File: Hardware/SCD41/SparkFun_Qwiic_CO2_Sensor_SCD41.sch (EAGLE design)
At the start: 26 parts, among them J1 QWIIC_RA, J2 QWIIC_RA, J3 PTH, U1 SCD40/1, U6 SCD40, U7 SCD41

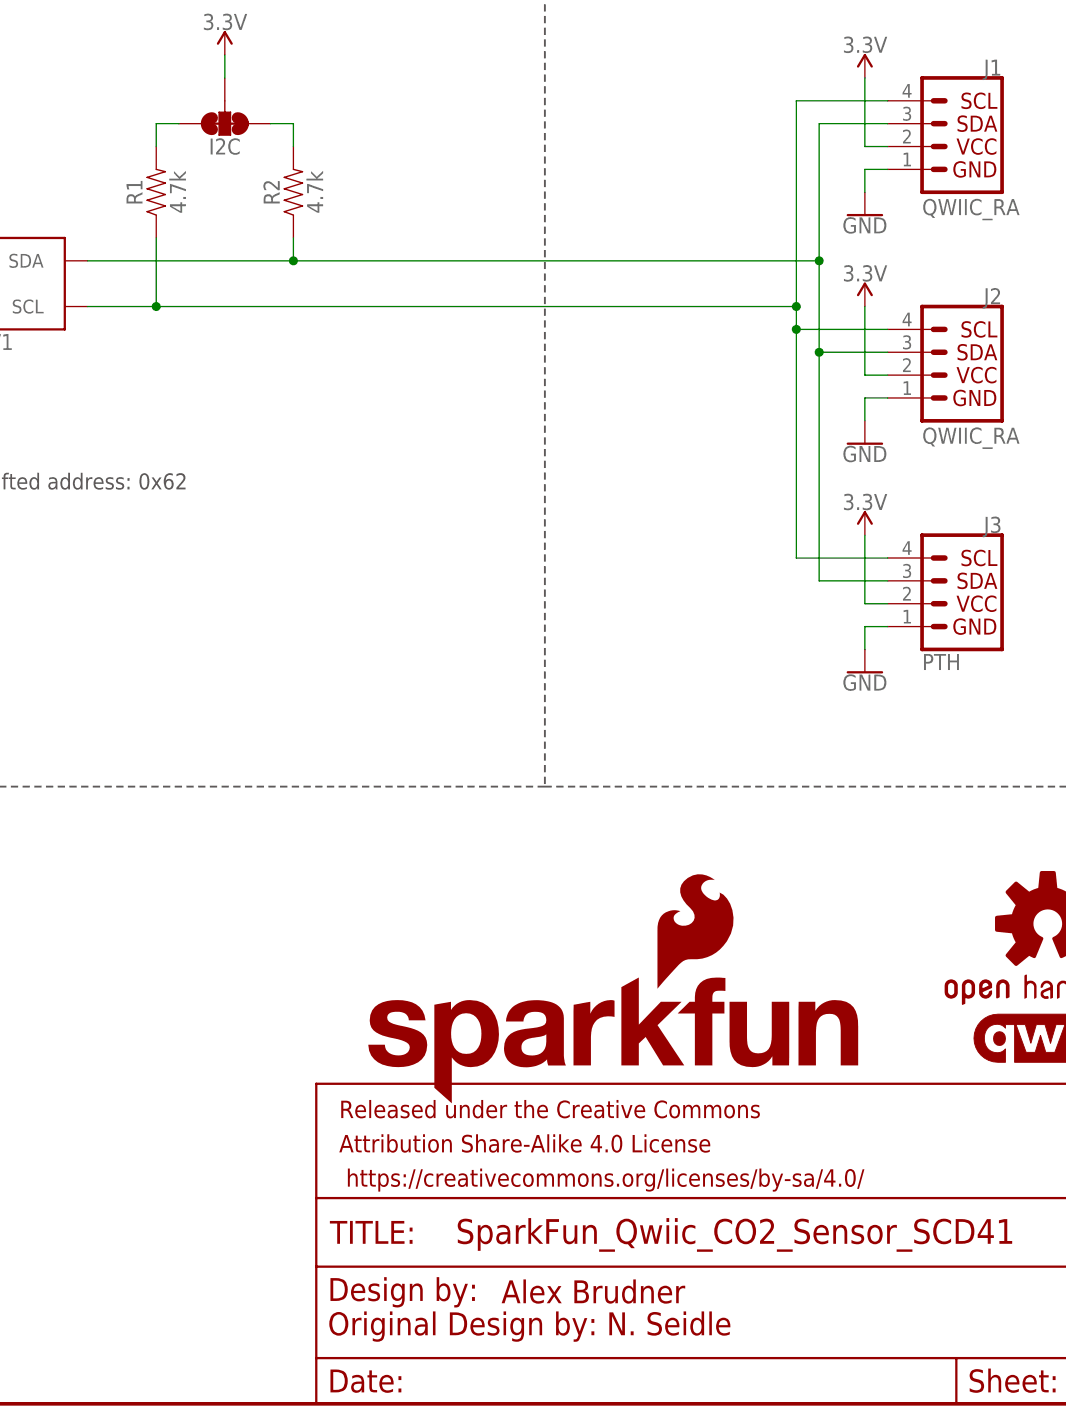
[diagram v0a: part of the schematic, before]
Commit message: Update from pre-design review notes.
Changed I2C PURs from 4.7k to 2.2k to match Qwiic standards.
Changed wording on revision.
Update top stop of pin 1 of sensor.
Repanelize.
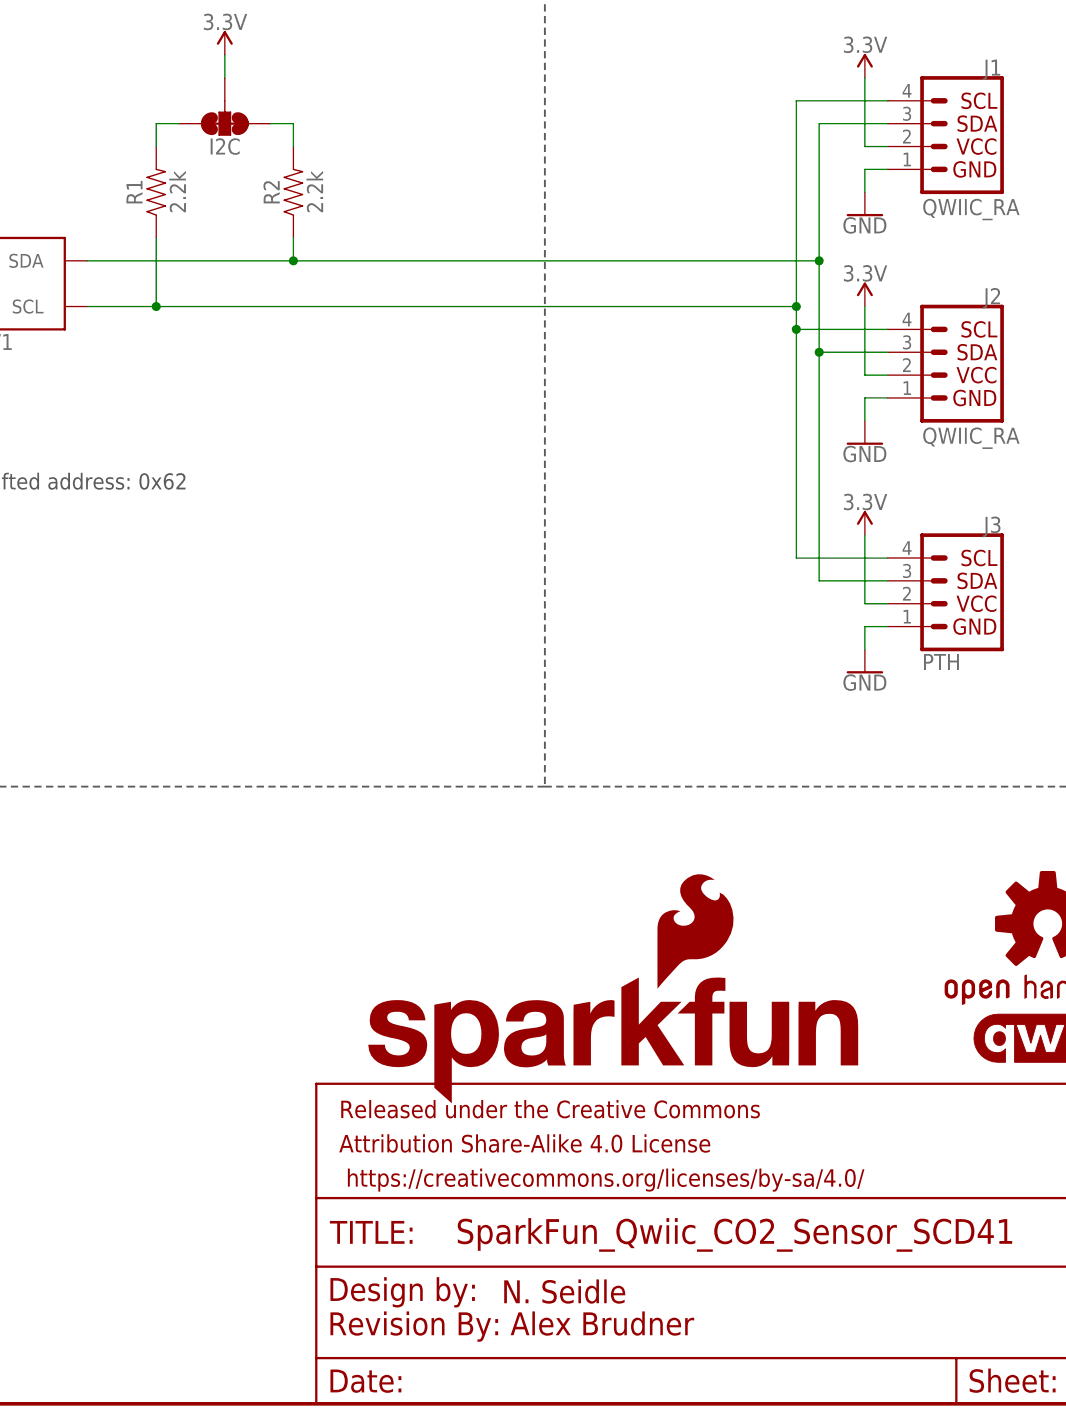
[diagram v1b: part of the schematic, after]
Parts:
- FRAME1: BASEDON Original Design by: N. Seidle -> Revision By: Alex Brudner; DESIGNER Alex Brudner -> N. Seidle
- R1, R2: value 4.7k -> 2.2k; device SparkFun-Resistors:4.7KOHM-0603-1/10W-1% -> SparkFun-Resistors:2.2KOHM-0603-1/10W-1%
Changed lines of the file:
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@@
 <parts>
 <part name="FRAME1" library="SparkFun-Aesthetics" deviceset="FRAME-LETTER" device="">
-<attribute name="BASEDON" value="Original Design by: N. Seidle"/>
-<attribute name="DESIGNER" value="Alex Brudner"/>
+<attribute name="BASEDON" value="Revision By: Alex Brudner"/>
+<attribute name="DESIGNER" value="N. Seidle"/>
 <attribute name="REV" value="v10"/>
 </part>
@@
 <part name="SUPPLY1" library="SparkFun-PowerSymbols" deviceset="3.3V" device=""/>
 <part name="SUPPLY2" library="SparkFun-PowerSymbols" deviceset="3.3V" device=""/>
-<part name="R1" library="SparkFun-Resistors" deviceset="4.7KOHM" device="-0603-1/10W-1%" value="4.7k"/>
-<part name="R2" library="SparkFun-Resistors" deviceset="4.7KOHM" device="-0603-1/10W-1%" value="4.7k"/>
+<part name="R1" library="SparkFun-Resistors" deviceset="2.2KOHM" device="-0603-1/10W-1%" value="2.2k"/>
+<part name="R2" library="SparkFun-Resistors" deviceset="2.2KOHM" device="-0603-1/10W-1%" value="2.2k"/>
 <part name="J3" library="SparkFun-Connectors" deviceset="I2C_STANDARD" device="_NO_SILK" value="PTH"/>
 <part name="GND3" library="SparkFun-PowerSymbols" deviceset="GND" device=""/>
@@
 <wire x1="58.42" y1="68.58" x2="58.42" y2="0" width="0.2032" layer="97" style="longdash"/>
 <text x="30.48" y="55.88" size="3.048" layer="94" font="vector" align="bottom-center">Part Number</text>
-<text x="116.84" y="165.1" size="1.778" layer="97" align="bottom-center">Input: 2.4V-5.5V
+<text x="116.84" y="165.1" size="1.778" layer="97" font="vector" align="bottom-center">Input: 2.4V-5.5V
 This board runs 3.3V only.</text>
 <text x="116.84" y="101.6" size="1.778" layer="97" font="vector" align="bottom-center">7-bit unshifted address: 0x62</text>
@@
 <instance part="H4" gate="G$1" x="243.84" y="27.94" smashed="yes"/>
 <instance part="U1" gate="U1" x="111.76" y="124.46" smashed="yes">
-<attribute name="NAME" x="104.14" y="130.048" size="1.778" layer="95"/>
-<attribute name="VALUE" x="104.14" y="117.094" size="1.778" layer="96"/>
+<attribute name="NAME" x="104.14" y="130.048" size="1.778" layer="95" font="vector"/>
+<attribute name="VALUE" x="104.14" y="117.094" size="1.778" layer="96" font="vector"/>
 </instance>
 <instance part="J1" gate="G$1" x="218.44" y="139.7" smashed="yes" rot="MR0">
